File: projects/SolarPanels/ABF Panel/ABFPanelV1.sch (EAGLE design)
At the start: 47 parts

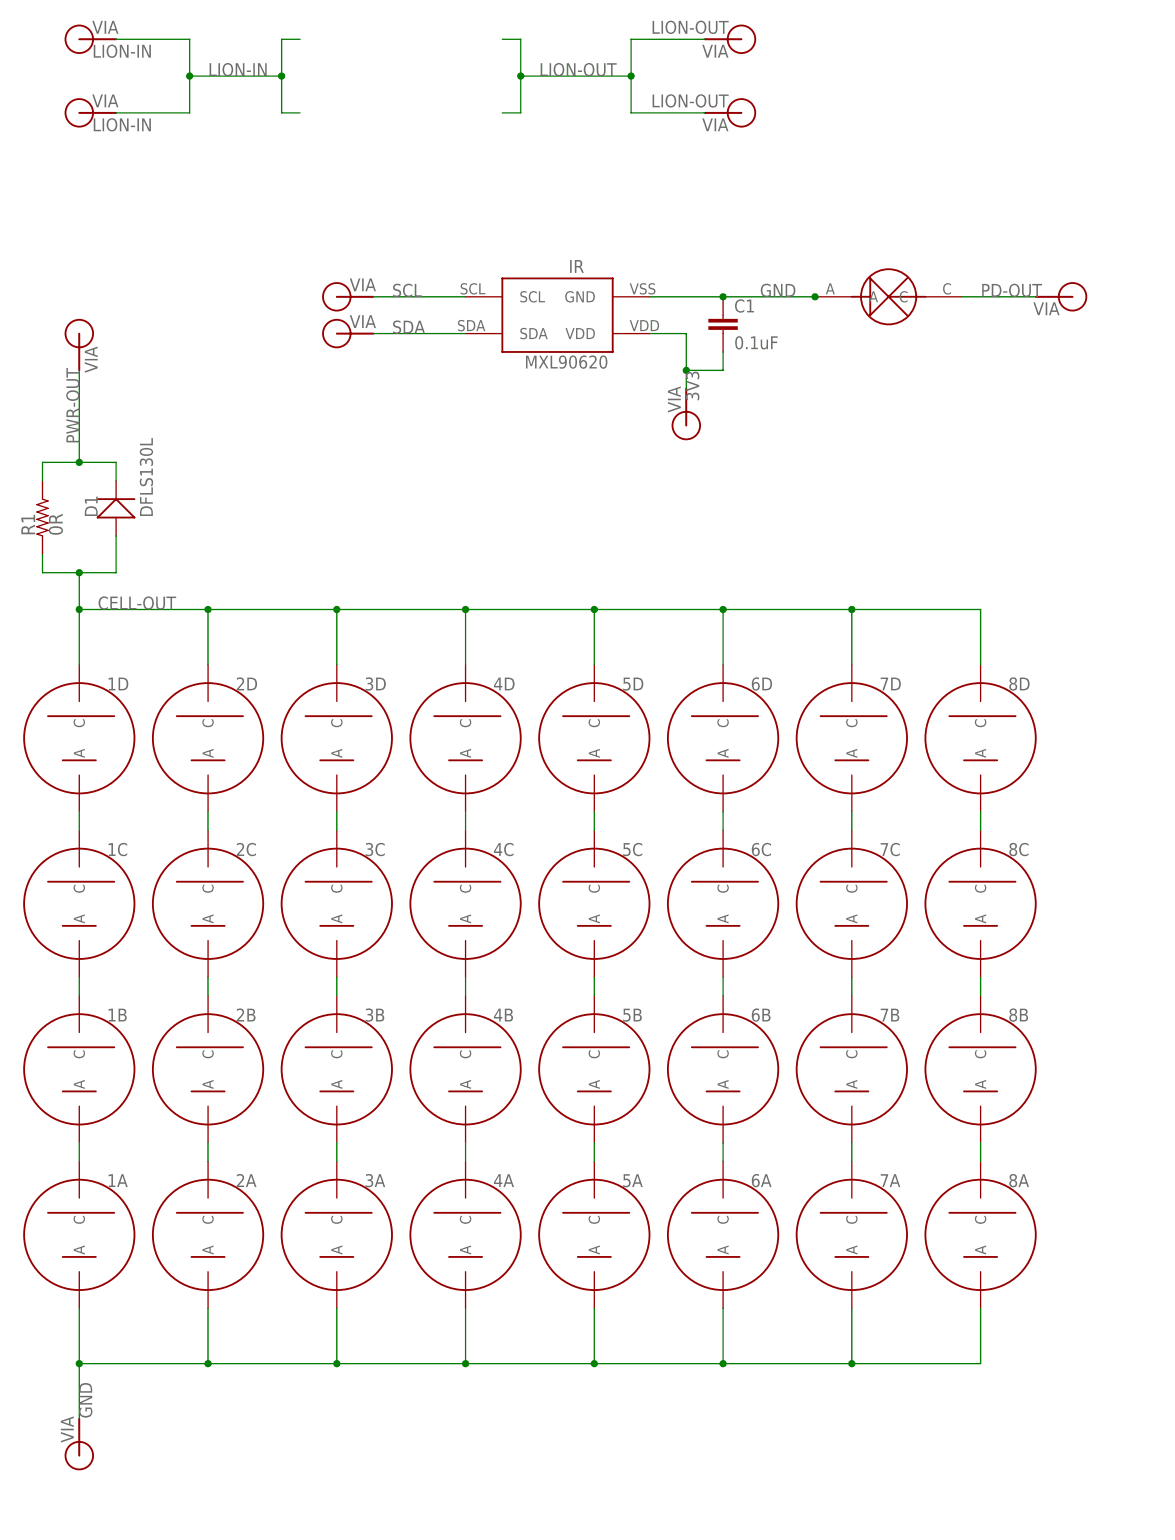
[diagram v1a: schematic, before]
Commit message: Continued work on ABFPanelV1. Just needs final selection on ABF mechanism. Room already allocated on panel for it.
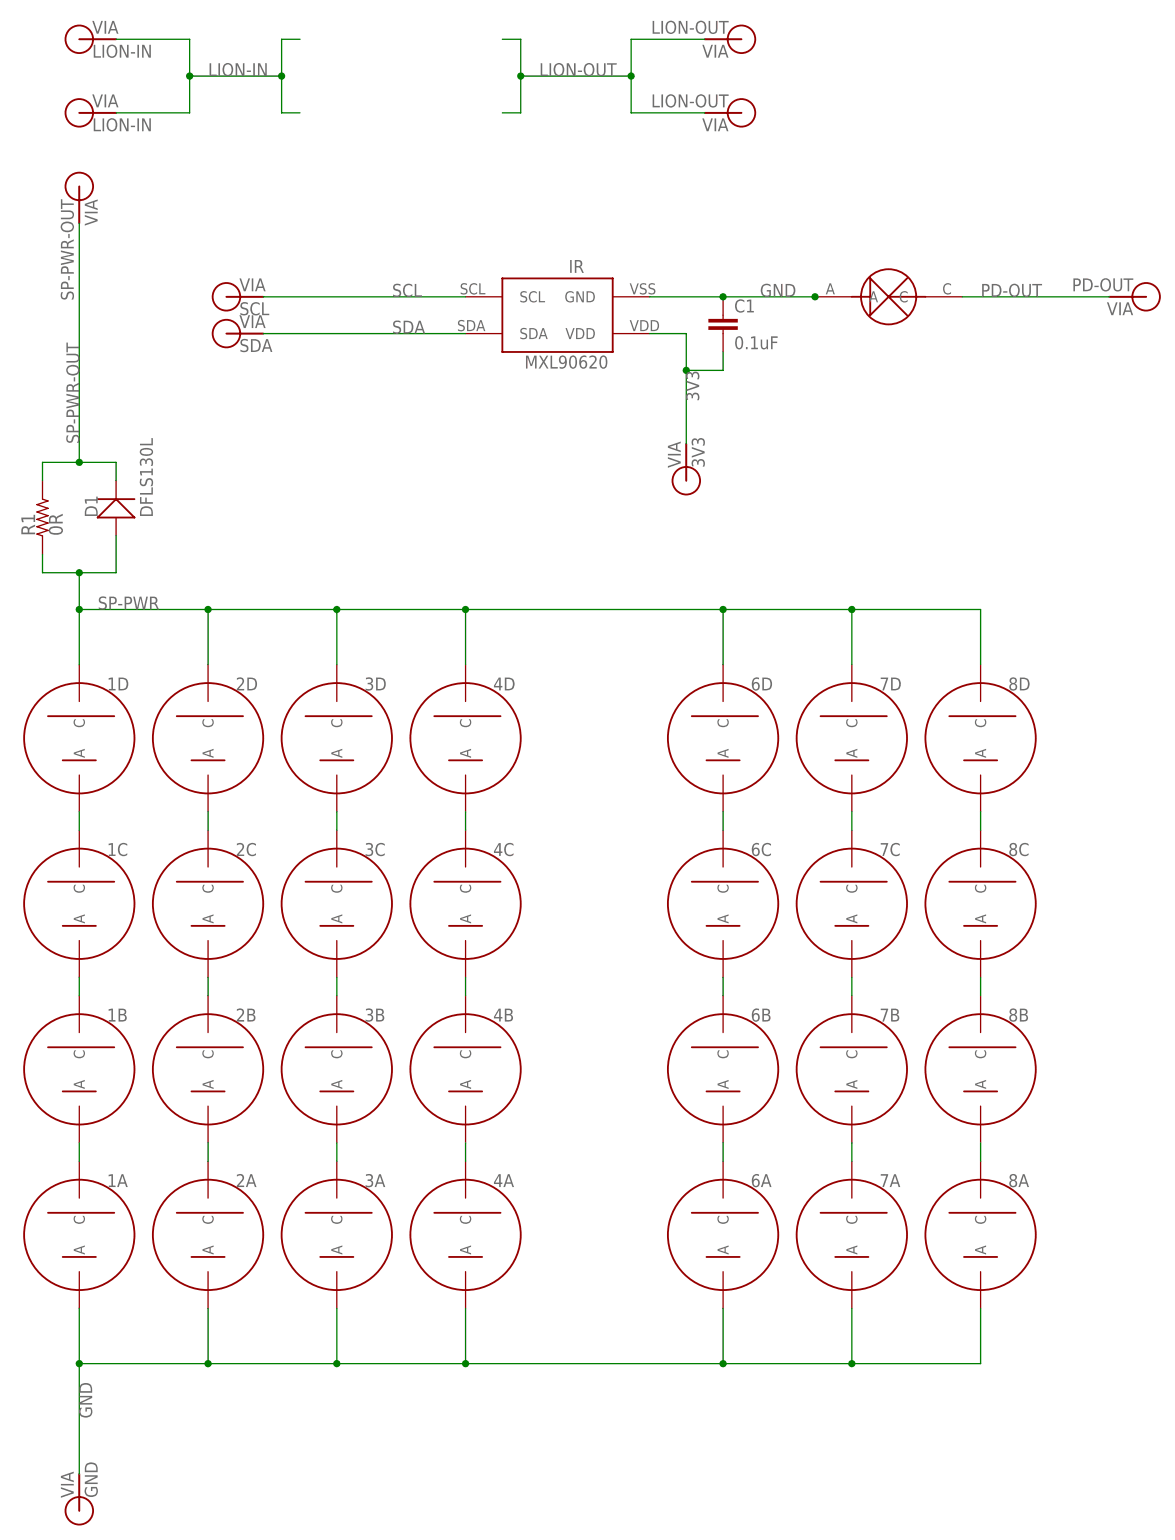
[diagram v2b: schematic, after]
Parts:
- removed 5A, 5B, 5C, 5D: SOLARCELLV3, BrownSpaceEngineering:SOLARCELLV3
- 3V3: value (none) -> 3V3
- GND: value (none) -> GND
- PD-OUT: value (none) -> PD-OUT
- PWR-OUT: value (none) -> SP-PWR-OUT
- SCL: value (none) -> SCL
- SDA: value (none) -> SDA
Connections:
- net PWR-OUT renamed SP-PWR-OUT
- removed net CELL-OUT: 1D.C, 2D.C, 3D.C, 4D.C, 5D.C, 6D.C, 7D.C, 8D.C, D1.A, R1.1
- removed net N$13: 5C.C, 5D.A
- removed net N$15: 5B.C, 5C.A
- removed net N$16: 5A.C, 5B.A
- new net SP-PWR: 1D.C, 2D.C, 3D.C, 4D.C, 6D.C, 7D.C, 8D.C, D1.A, R1.1
- net GND: no longer 5A.A
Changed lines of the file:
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@@
 <part name="4B" library="BrownSpaceEngineering" deviceset="SOLARCELLV3" device=""/>
 <part name="4A" library="BrownSpaceEngineering" deviceset="SOLARCELLV3" device=""/>
-<part name="5D" library="BrownSpaceEngineering" deviceset="SOLARCELLV3" device=""/>
-<part name="5C" library="BrownSpaceEngineering" deviceset="SOLARCELLV3" device=""/>
-<part name="5B" library="BrownSpaceEngineering" deviceset="SOLARCELLV3" device=""/>
-<part name="5A" library="BrownSpaceEngineering" deviceset="SOLARCELLV3" device=""/>
 <part name="6D" library="BrownSpaceEngineering" deviceset="SOLARCELLV3" device=""/>
 <part name="6C" library="BrownSpaceEngineering" deviceset="SOLARCELLV3" device=""/>
@@
 <part name="8B" library="BrownSpaceEngineering" deviceset="SOLARCELLV3" device=""/>
 <part name="8A" library="BrownSpaceEngineering" deviceset="SOLARCELLV3" device=""/>
-<part name="SCL" library="BrownSpaceEngineering" deviceset="VIA" device="-60MIL"/>
-<part name="SDA" library="BrownSpaceEngineering" deviceset="VIA" device="-60MIL"/>
-<part name="PD-OUT" library="BrownSpaceEngineering" deviceset="VIA" device="-60MIL"/>
-<part name="3V3" library="BrownSpaceEngineering" deviceset="VIA" device="-60MIL"/>
-<part name="PWR-OUT" library="BrownSpaceEngineering" deviceset="VIA" device="-60MIL"/>
-<part name="GND" library="BrownSpaceEngineering" deviceset="VIA" device="-60MIL"/>
+<part name="SCL" library="BrownSpaceEngineering" deviceset="VIA" device="-60MIL" value="SCL"/>
+<part name="SDA" library="BrownSpaceEngineering" deviceset="VIA" device="-60MIL" value="SDA"/>
+<part name="PD-OUT" library="BrownSpaceEngineering" deviceset="VIA" device="-60MIL" value="PD-OUT"/>
+<part name="3V3" library="BrownSpaceEngineering" deviceset="VIA" device="-60MIL" value="3V3"/>
+<part name="PWR-OUT" library="BrownSpaceEngineering" deviceset="VIA" device="-60MIL" value="SP-PWR-OUT"/>
+<part name="GND" library="BrownSpaceEngineering" deviceset="VIA" device="-60MIL" value="GND"/>
 <part name="D1" library="BrownSpaceEngineering" deviceset="DFLS130L" device="" value="DFLS130L"/>
 <part name="R1" library="BrownSpaceEngineering" deviceset="RES" device="1210" value="0R"/>
@@
 <instance part="4B" gate="G$1" x="-91.44" y="0"/>
 <instance part="4A" gate="G$1" x="-91.44" y="-22.86"/>
-<instance part="5D" gate="G$1" x="-73.66" y="45.72"/>
-<instance part="5C" gate="G$1" x="-73.66" y="22.86"/>
-<instance part="5B" gate="G$1" x="-73.66" y="0"/>
-<instance part="5A" gate="G$1" x="-73.66" y="-22.86"/>
 <instance part="6D" gate="G$1" x="-55.88" y="45.72"/>
 <instance part="6C" gate="G$1" x="-55.88" y="22.86"/>
@@
 <instance part="8B" gate="G$1" x="-20.32" y="0"/>
 <instance part="8A" gate="G$1" x="-20.32" y="-22.86"/>
-<instance part="SCL" gate="G$1" x="-109.22" y="106.68"/>
-<instance part="SDA" gate="G$1" x="-109.22" y="101.6"/>
-<instance part="PD-OUT" gate="G$1" x="-7.62" y="106.68" rot="R180"/>
-<instance part="3V3" gate="G$1" x="-60.96" y="88.9" rot="R90"/>
-<instance part="PWR-OUT" gate="G$1" x="-144.78" y="101.6" smashed="yes" rot="R270">
-<attribute name="VALUE" x="-147.32" y="99.822" size="1.778" layer="96" rot="R270"/>
+<instance part="SCL" gate="G$1" x="-124.46" y="106.68"/>
+<instance part="SDA" gate="G$1" x="-124.46" y="101.6"/>
+<instance part="PD-OUT" gate="G$1" x="2.54" y="106.68" rot="R180"/>
+<instance part="3V3" gate="G$1" x="-60.96" y="81.28" rot="R90"/>
+<instance part="PWR-OUT" gate="G$1" x="-144.78" y="121.92" smashed="yes" rot="R270">
+<attribute name="VALUE" x="-147.32" y="120.142" size="1.778" layer="96" rot="R270"/>
 </instance>
-<instance part="GND" gate="G$1" x="-144.78" y="-53.34" rot="R90"/>
+<instance part="GND" gate="G$1" x="-144.78" y="-60.96" rot="R90"/>
 <instance part="D1" gate="G$1" x="-139.7" y="76.2" rot="R90"/>
 <instance part="R1" gate="R$1" x="-149.86" y="76.2" rot="R90"/>
@@
 <pinref part="7A" gate="G$1" pin="A"/>
 <wire x1="-38.1" y1="-40.64" x2="-55.88" y2="-40.64" width="0.1524" layer="91"/>
-<wire x1="-55.88" y1="-40.64" x2="-73.66" y2="-40.64" width="0.1524" layer="91"/>
-<wire x1="-73.66" y1="-40.64" x2="-91.44" y2="-40.64" width="0.1524" layer="91"/>
+<wire x1="-55.88" y1="-40.64" x2="-91.44" y2="-40.64" width="0.1524" layer="91"/>
 <wire x1="-91.44" y1="-40.64" x2="-109.22" y2="-40.64" width="0.1524" layer="91"/>
 <wire x1="-109.22" y1="-40.64" x2="-127" y2="-40.64" width="0.1524" layer="91"/>
@@
 <wire x1="-55.88" y1="-33.02" x2="-55.88" y2="-40.64" width="0.1524" layer="91"/>
 <junction x="-55.88" y="-40.64"/>
-<pinref part="5A" gate="G$1" pin="A"/>
-<wire x1="-73.66" y1="-33.02" x2="-73.66" y2="-40.64" width="0.1524" layer="91"/>
-<junction x="-73.66" y="-40.64"/>
 <pinref part="4A" gate="G$1" pin="A"/>
 <wire x1="-91.44" y1="-33.02" x2="-91.44" y2="-40.64" width="0.1524" layer="91"/>
@@
 <wire x1="-127" y1="-33.02" x2="-127" y2="-40.64" width="0.1524" layer="91"/>
 <junction x="-127" y="-40.64"/>
-<wire x1="-144.78" y1="-40.64" x2="-144.78" y2="-48.26" width="0.1524" layer="91"/>
+<wire x1="-144.78" y1="-40.64" x2="-144.78" y2="-55.88" width="0.1524" layer="91"/>
 <junction x="-144.78" y="-40.64"/>
 <pinref part="GND" gate="G$1" pin="P$1"/>
@@
 <segment>
 <pinref part="IR" gate="G$1" pin="SDA"/>
-<wire x1="-91.44" y1="101.6" x2="-104.14" y2="101.6" width="0.1524" layer="91"/>
+<wire x1="-91.44" y1="101.6" x2="-119.38" y2="101.6" width="0.1524" layer="91"/>
 <label x="-101.6" y="101.6" size="1.778" layer="95"/>
 <pinref part="SDA" gate="G$1" pin="P$1"/>
@@
 <segment>
 <pinref part="IR" gate="G$1" pin="SCL"/>
-<wire x1="-91.44" y1="106.68" x2="-104.14" y2="106.68" width="0.1524" layer="91"/>
+<wire x1="-91.44" y1="106.68" x2="-119.38" y2="106.68" width="0.1524" layer="91"/>
 <label x="-101.6" y="106.68" size="1.778" layer="95"/>
 <pinref part="SCL" gate="G$1" pin="P$1"/>
@@
 <wire x1="-60.96" y1="101.6" x2="-60.96" y2="96.52" width="0.1524" layer="91"/>
 <pinref part="C1" gate="G$1" pin="2"/>
-<wire x1="-60.96" y1="96.52" x2="-60.96" y2="93.98" width="0.1524" layer="91"/>
+<wire x1="-60.96" y1="96.52" x2="-60.96" y2="86.36" width="0.1524" layer="91"/>
 <wire x1="-60.96" y1="96.52" x2="-55.88" y2="96.52" width="0.1524" layer="91"/>
 <wire x1="-55.88" y1="96.52" x2="-55.88" y2="99.06" width="0.1524" layer="91"/>
@@
 <segment>
 <pinref part="PD" gate="G$1" pin="C"/>
-<wire x1="-22.86" y1="106.68" x2="-12.7" y2="106.68" width="0.1524" layer="91"/>
+<wire x1="-22.86" y1="106.68" x2="-2.54" y2="106.68" width="0.1524" layer="91"/>
 <label x="-20.32" y="106.68" size="1.778" layer="95"/>
 <pinref part="PD-OUT" gate="G$1" pin="P$1"/>
@@
 </segment>
 </net>
-<net name="N$13" class="0">
-<segment>
-<pinref part="5D" gate="G$1" pin="A"/>
-<pinref part="5C" gate="G$1" pin="C"/>
-<wire x1="-73.66" y1="35.56" x2="-73.66" y2="33.02" width="0.1524" layer="91"/>
-</segment>
-</net>
-<net name="N$15" class="0">
-<segment>
-<pinref part="5C" gate="G$1" pin="A"/>
-<pinref part="5B" gate="G$1" pin="C"/>
-<wire x1="-73.66" y1="12.7" x2="-73.66" y2="10.16" width="0.1524" layer="91"/>
-</segment>
-</net>
-<net name="N$16" class="0">
-<segment>
-<pinref part="5B" gate="G$1" pin="A"/>
-<pinref part="5A" gate="G$1" pin="C"/>
-<wire x1="-73.66" y1="-10.16" x2="-73.66" y2="-12.7" width="0.1524" layer="91"/>
-</segment>
-</net>
 <net name="N$17" class="0">
 <segment>
@@
 </segment>
 </net>
-<net name="CELL-OUT" class="0">
+<net name="SP-PWR" class="0">
 <segment>
 <pinref part="7D" gate="G$1" pin="C"/>
@@
 <pinref part="6D" gate="G$1" pin="C"/>
 <wire x1="-55.88" y1="55.88" x2="-55.88" y2="63.5" width="0.1524" layer="91"/>
-<pinref part="5D" gate="G$1" pin="C"/>
-<wire x1="-73.66" y1="55.88" x2="-73.66" y2="63.5" width="0.1524" layer="91"/>
 <pinref part="4D" gate="G$1" pin="C"/>
 <wire x1="-91.44" y1="55.88" x2="-91.44" y2="63.5" width="0.1524" layer="91"/>
@@
 <junction x="-91.44" y="63.5"/>
 <wire x1="-38.1" y1="63.5" x2="-55.88" y2="63.5" width="0.1524" layer="91"/>
-<wire x1="-55.88" y1="63.5" x2="-73.66" y2="63.5" width="0.1524" layer="91"/>
-<wire x1="-73.66" y1="63.5" x2="-91.44" y2="63.5" width="0.1524" layer="91"/>
+<wire x1="-55.88" y1="63.5" x2="-91.44" y2="63.5" width="0.1524" layer="91"/>
 <wire x1="-91.44" y1="63.5" x2="-109.22" y2="63.5" width="0.1524" layer="91"/>
-<junction x="-73.66" y="63.5"/>
 <junction x="-55.88" y="63.5"/>
 <junction x="-38.1" y="63.5"/>
@@
 </segment>
 </net>
-<net name="PWR-OUT" class="0">
+<net name="SP-PWR-OUT" class="0">
 <segment>
 <pinref part="R1" gate="R$1" pin="2"/>
@@
 <pinref part="PWR-OUT" gate="G$1" pin="P$1"/>
 <wire x1="-144.78" y1="83.82" x2="-149.86" y2="83.82" width="0.1524" layer="91"/>
-<wire x1="-144.78" y1="83.82" x2="-144.78" y2="96.52" width="0.1524" layer="91"/>
+<wire x1="-144.78" y1="83.82" x2="-144.78" y2="116.84" width="0.1524" layer="91"/>
 <junction x="-144.78" y="83.82"/>
 <label x="-144.78" y="86.36" size="1.778" layer="95" rot="R90"/>
